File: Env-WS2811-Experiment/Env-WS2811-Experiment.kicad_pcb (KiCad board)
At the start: 2 copper layers, 131.1 x 29 mm, 142 parts, among them J1 Conn_01x04, Q1 Si2301DS, Q10 Si2301DS, Q11 Si2301DS, Q12 Si2301DS, Q13 Si2301DS, Q14 Si2301DS, Q15 Si2301DS, Q16 Si2301DS, Q17 Si2301DS, Q18 Si2301DS, Q19 Si2301DS, Q2 Si2301DS, Q20 Si2301DS, Q21 Si2301DS, Q22 Si2301DS, Q23 Si2301DS, Q24 Si2301DS, Q25 Si2301DS, Q26 Si2301DS, Q27 Si2301DS, Q28 Si2301DS, Q29 Si2301DS, Q3 Si2301DS, Q30 Si2301DS, Q31 Si2301DS, Q32 Si2301DS, Q33 Si2301DS, Q34 Si2301DS, Q35 Si2301DS, Q36 Si2301DS, Q4 Si2301DS, Q5 Si2301DS, Q6 Si2301DS, Q7 Si2301DS, Q8 Si2301DS, Q9 Si2301DS, U1 WS2811, U10 WS2811, U11 WS2811, U12 WS2811, U2 WS2811, U3 WS2811, U4 WS2811, U5 WS2811, U6 WS2811, U7 WS2811, U8 WS2811, U9 WS2811

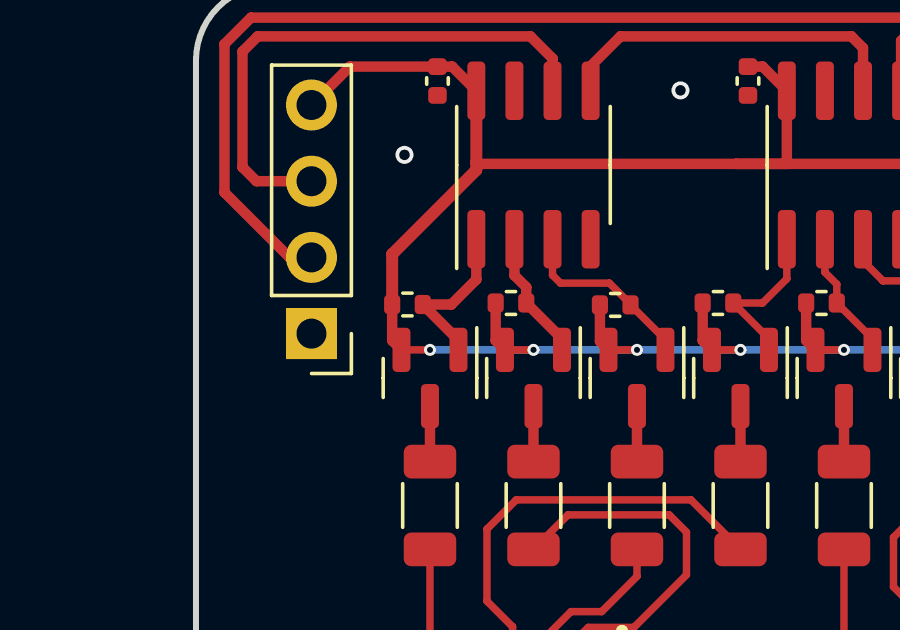
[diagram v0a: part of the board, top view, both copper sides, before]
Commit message: swap some mosfets over to more compact versions
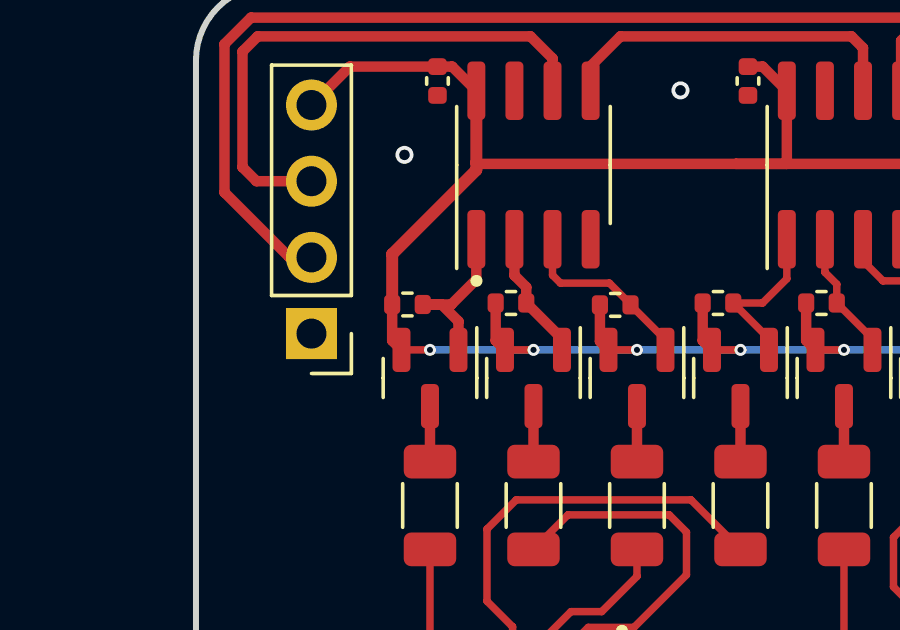
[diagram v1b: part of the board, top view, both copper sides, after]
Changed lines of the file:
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@@
     )
   )
+  (gr_circle (center 29.85 35.1) (end 30 35.1)
+    (stroke (width 0.1) (type solid)) (fill solid) (layer "F.SilkS"))
   (gr_arc (start 23 54.2) (mid 21.232233 53.467767) (end 20.5 51.7)
     (stroke (width 0.2) (type default)) (layer "Edge.Cuts"))
@@
   (segment (start 83.45 37.4) (end 87 37.4) (width 0.25) (layer "B.Cu") (net 19))
   (segment (start 29.845 35.055) (end 29.845 33.7125) (width 0.35) (layer "F.Cu") (net 20))
-  (segment (start 29.25 37.4) (end 29.25 37.0775) (width 0.35) (layer "F.Cu") (net 20))
-  (segment (start 29.25 37.0775) (end 28.06 35.8875) (width 0.35) (layer "F.Cu") (net 20))
+  (segment (start 29.25 37.4) (end 29.25 36.45) (width 0.35) (layer "F.Cu") (net 20))
+  (segment (start 29.25 36.45) (end 28.6875 35.8875) (width 0.35) (layer "F.Cu") (net 20))
   (segment (start 29.0125 35.8875) (end 29.845 35.055) (width 0.35) (layer "F.Cu") (net 20))
   (segment (start 28.06 35.8875) (end 29.0125 35.8875) (width 0.35) (layer "F.Cu") (net 20))
+  (segment (start 28.6875 35.8875) (end 28.06 35.8875) (width 0.35) (layer "F.Cu") (net 20))
   (segment (start 28.3 39.275) (end 28.3 41.125) (width 0.35) (layer "F.Cu") (net 21))
   (segment (start 32.7 37.4) (end 32.7 37.0275) (width 0.35) (layer "F.Cu") (net 22))
